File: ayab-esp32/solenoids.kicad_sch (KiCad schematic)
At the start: 10 parts, among them U301 MCP23017_SS

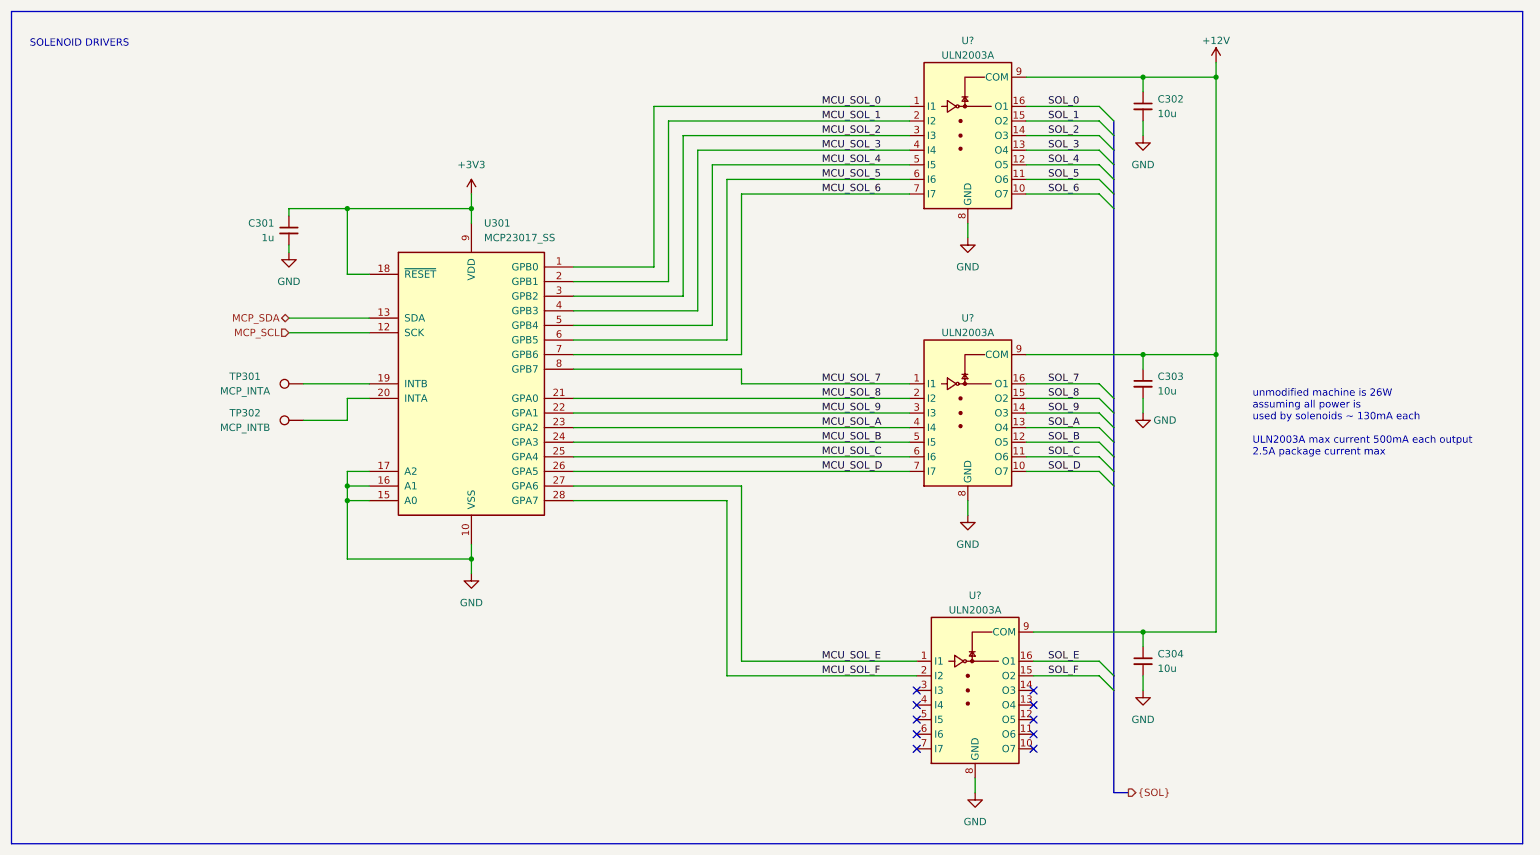
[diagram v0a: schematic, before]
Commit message: add component selection, bom
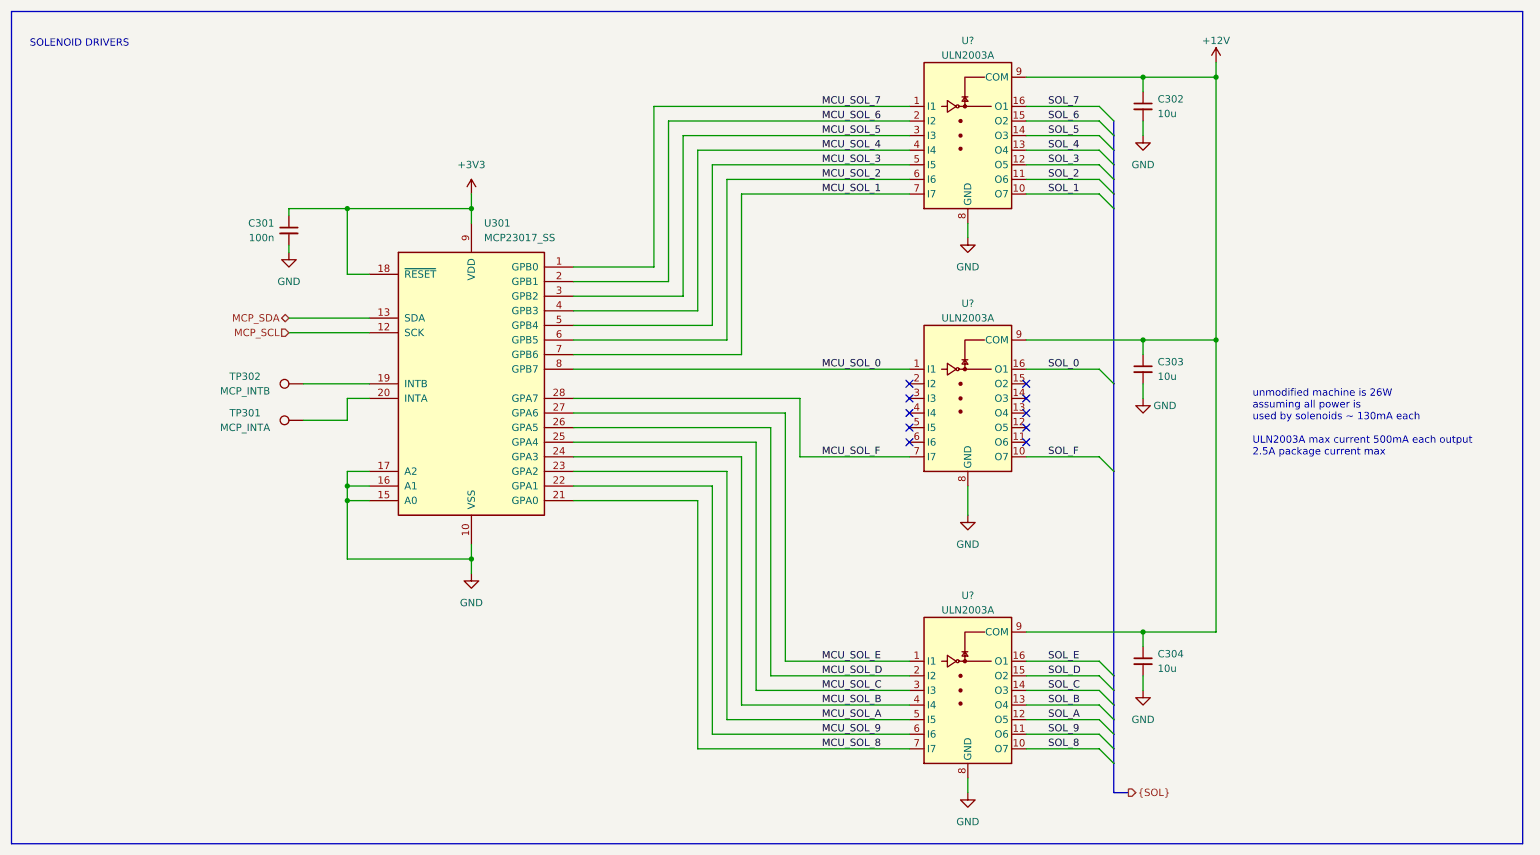
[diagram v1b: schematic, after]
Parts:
- C301: value 1u -> 100n; footprint (none) -> Capacitor_SMD:C_0603_1608Metric; symbol ayab-esp32:C_Small -> Library:C_Small; LCSC ID (none) -> C57112; OEM (none) -> FH (Guangdong Fenghua Advanced Tech); OEM PN (none) -> 0603B103K500NT; Package (none) -> 0603; Voltage rating (none) -> 24V X7R
- C302, C303, C304: footprint (none) -> Capacitor_SMD:C_0805_2012Metric; symbol ayab-esp32:C_Small -> Library:C_Small; LCSC ID (none) -> C15850; OEM (none) -> Samsung Electro-Mechanics; OEM PN (none) -> CL21A106KAYNNNE; Package (none) -> 0805; Voltage rating (none) -> 24V X5R
- TP301, TP302: footprint (none) -> TestPoint:TestPoint_Pad_D2.0mm; symbol ayab-esp32:TestPoint -> Library:TestPoint; now left out of the parts list
- U301: symbol ayab-esp32:MCP23017_SS -> Library:MCP23017_SS; LCSC ID (none) -> C506653; OEM (none) -> Microchip Tech; OEM PN (none) -> MCP23017-E/SS; Package (none) -> SSOP-28
- U? (x3): symbol ayab-esp32:ULN2003A -> Library:ULN2003A; LCSC ID (none) -> C7512; OEM (none) -> Texas Instruments; OEM PN (none) -> ULN2003ADR; Package (none) -> SOIC-16
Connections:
- net MCU_SOL_0: now also U301.8 (GPB7), U?.1 (I1); no longer U301.1 (GPB0), U?.1 (I1)
- net MCU_SOL_1: now also U301.7 (GPB6), U?.7 (I7); no longer U301.2 (GPB1), U?.2 (I2)
- net MCU_SOL_2: now also U301.6 (GPB5), U?.6 (I6); no longer U301.3 (GPB2), U?.3 (I3)
- net MCU_SOL_3: now also U301.5 (GPB4), U?.5 (I5); no longer U301.4 (GPB3), U?.4 (I4)
- net MCU_SOL_4: now also U301.4 (GPB3), U?.4 (I4); no longer U301.5 (GPB4), U?.5 (I5)
- net MCU_SOL_5: now also U301.3 (GPB2), U?.3 (I3); no longer U301.6 (GPB5), U?.6 (I6)
- net MCU_SOL_6: now also U301.2 (GPB1), U?.2 (I2); no longer U301.7 (GPB6), U?.7 (I7)
- net MCU_SOL_7: now also U301.1 (GPB0), U?.1 (I1); no longer U301.8 (GPB7), U?.1 (I1)
- net MCU_SOL_8: now also U?.7 (I7); no longer U?.2 (I2)
- net MCU_SOL_9: now also U?.6 (I6); no longer U?.3 (I3)
- net MCU_SOL_A: now also U?.5 (I5); no longer U?.4 (I4)
- net MCU_SOL_B: now also U?.4 (I4); no longer U?.5 (I5)
- net MCU_SOL_C: now also U?.3 (I3); no longer U?.6 (I6)
- net MCU_SOL_D: now also U?.2 (I2); no longer U?.7 (I7)
- net MCU_SOL_F: now also U?.7 (I7); no longer U?.2 (I2)
- net SOL_0: now also U?.16 (O1); no longer U?.16 (O1)
- net SOL_1: now also U?.10 (O7); no longer U?.15 (O2)
- net SOL_2: now also U?.11 (O6); no longer U?.14 (O3)
- net SOL_3: now also U?.12 (O5); no longer U?.13 (O4)
- net SOL_4: now also U?.13 (O4); no longer U?.12 (O5)
- net SOL_5: now also U?.14 (O3); no longer U?.11 (O6)
- net SOL_6: now also U?.15 (O2); no longer U?.10 (O7)
- net SOL_7: now also U?.16 (O1); no longer U?.16 (O1)
- net SOL_8: now also U?.10 (O7); no longer U?.15 (O2)
- net SOL_9: now also U?.11 (O6); no longer U?.14 (O3)
- net SOL_A: now also U?.12 (O5); no longer U?.13 (O4)
- net SOL_B: now also U?.13 (O4); no longer U?.12 (O5)
- net SOL_C: now also U?.14 (O3); no longer U?.11 (O6)
- net SOL_D: now also U?.15 (O2); no longer U?.10 (O7)
- net SOL_F: now also U?.10 (O7); no longer U?.15 (O2)
- net at U301.19 (INTB): now also TP302.1; no longer TP301.1
- net at U301.20 (INTA): now also TP301.1; no longer TP302.1
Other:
- moved on the sheet: C303, TP301, TP302, U?

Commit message: review ZVD P-ch MOSFET and resistors
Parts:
- C301, C302, C303, C304: symbol Library:C_Small -> ayab-lib:C_Small
- TP301, TP302: symbol Library:TestPoint -> ayab-lib:TestPoint
- U301: symbol Library:MCP23017_SS -> ayab-lib:MCP23017_SS
- U? (x3): symbol Library:ULN2003A -> ayab-lib:ULN2003A
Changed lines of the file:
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@@
     )
   )
-  (symbol (lib_id "Library:C_Small") (at 214.63 129.54 0) (unit 1)
+  (symbol (lib_id "ayab-lib:C_Small") (at 214.63 129.54 0) (unit 1)
     (in_bom yes) (on_board yes) (dnp no)
     (property "Reference" "C304" (at 217.17 128.2763 0)
@@
     )
   )
-  (symbol (lib_id "Library:C_Small") (at 214.63 33.02 0) (unit 1)
+  (symbol (lib_id "ayab-lib:C_Small") (at 214.63 33.02 0) (unit 1)
     (in_bom yes) (on_board yes) (dnp no)
     (property "Reference" "C302" (at 217.17 31.7563 0)
@@
     )
   )
-  (symbol (lib_id "Library:ULN2003A") (at 184.15 38.1 0) (unit 1)
+  (symbol (lib_id "ayab-lib:ULN2003A") (at 184.15 38.1 0) (unit 1)
     (in_bom yes) (on_board yes) (dnp no) (fields_autoplaced)
     (property "Reference" "U?" (at 184.15 21.59 0)
@@
     )
   )
-  (symbol (lib_id "Library:C_Small") (at 66.04 54.61 0) (mirror y) (unit 1)
+  (symbol (lib_id "ayab-lib:C_Small") (at 66.04 54.61 0) (mirror y) (unit 1)
     (in_bom yes) (on_board yes) (dnp no)
     (property "Reference" "C301" (at 63.5 53.3463 0)
@@
     )
   )
-  (symbol (lib_id "Library:C_Small") (at 214.63 78.74 0) (unit 1)
+  (symbol (lib_id "ayab-lib:C_Small") (at 214.63 78.74 0) (unit 1)
     (in_bom yes) (on_board yes) (dnp no)
     (property "Reference" "C303" (at 217.17 77.4763 0)
@@
     )
   )
-  (symbol (lib_id "Library:MCP23017_SS") (at 97.79 81.28 0) (unit 1)
+  (symbol (lib_id "ayab-lib:MCP23017_SS") (at 97.79 81.28 0) (unit 1)
     (in_bom yes) (on_board yes) (dnp no) (fields_autoplaced)
     (property "Reference" "U301" (at 99.9841 53.34 0)
@@
     )
   )
-  (symbol (lib_id "Library:ULN2003A") (at 184.15 83.82 0) (unit 1)
+  (symbol (lib_id "ayab-lib:ULN2003A") (at 184.15 83.82 0) (unit 1)
     (in_bom yes) (on_board yes) (dnp no) (fields_autoplaced)
     (property "Reference" "U?" (at 184.15 67.31 0)
@@
     )
   )
-  (symbol (lib_id "Library:TestPoint") (at 68.58 87.63 90) (unit 1)
+  (symbol (lib_id "ayab-lib:TestPoint") (at 68.58 87.63 90) (unit 1)
     (in_bom no) (on_board yes) (dnp no)
     (property "Reference" "TP301" (at 58.42 86.36 90)
@@
     )
   )
-  (symbol (lib_id "Library:ULN2003A") (at 184.15 134.62 0) (unit 1)
+  (symbol (lib_id "ayab-lib:ULN2003A") (at 184.15 134.62 0) (unit 1)
     (in_bom yes) (on_board yes) (dnp no) (fields_autoplaced)
     (property "Reference" "U?" (at 184.15 118.11 0)
@@
     )
   )
-  (symbol (lib_id "Library:TestPoint") (at 68.58 81.28 90) (unit 1)
+  (symbol (lib_id "ayab-lib:TestPoint") (at 68.58 81.28 90) (unit 1)
     (in_bom no) (on_board yes) (dnp no)
     (property "Reference" "TP302" (at 58.42 80.01 90)

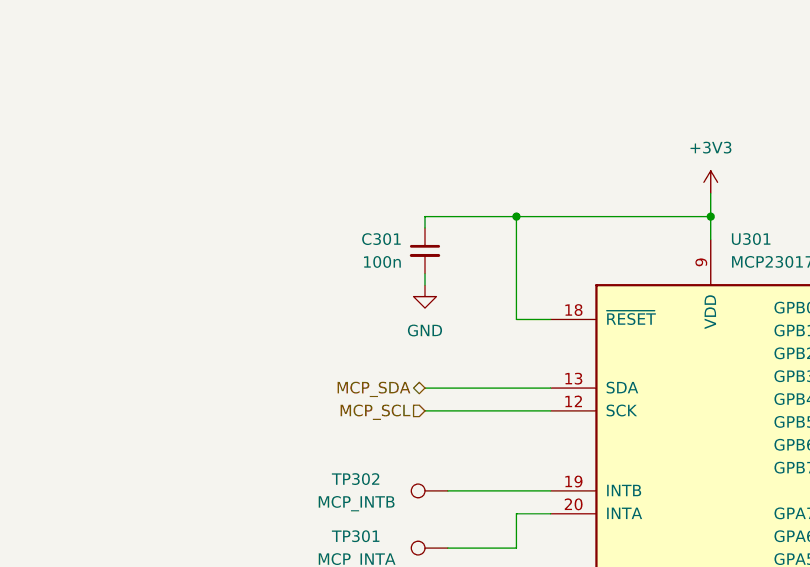
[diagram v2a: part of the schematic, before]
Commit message: first draft layout DRC clean
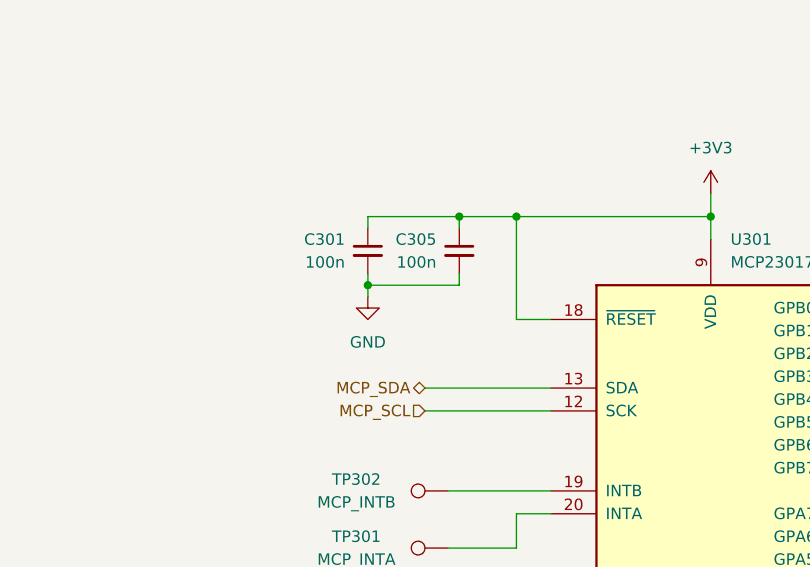
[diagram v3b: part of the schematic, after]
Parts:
- added C305: 100n, Capacitor_SMD:C_0603_1608Metric, symbol ayab-lib:C_Small
- TP301, TP302: footprint TestPoint:TestPoint_Pad_D2.0mm -> TestPoint:TestPoint_Pad_D1.0mm
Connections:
- net +3V3: now also C305.1
- net GND: now also C305.2
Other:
- moved on the sheet: C301
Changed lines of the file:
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@@
   (junction (at 97.79 111.76) (diameter 0) (color 0 0 0 0)
   )
+  (junction (at 59.69 58.42) (diameter 0) (color 0 0 0 0)
+  )
   (junction (at 76.2 101.6) (diameter 0) (color 0 0 0 0)
+  )
+  (junction (at 69.85 50.8) (diameter 0) (color 0 0 0 0)
   )
   (junction (at 227.33 73.66) (diameter 0) (color 0 0 0 0)
@@
     (stroke (width 0) (type default))
   )
+  (wire (pts (xy 69.85 57.15) (xy 69.85 58.42))
+    (stroke (width 0) (type default))
+  )
   (bus (pts (xy 209.55 96.52) (xy 209.55 132.08))
     (stroke (width 0) (type default))
@@
     (stroke (width 0) (type default))
   )
+  (wire (pts (xy 59.69 58.42) (xy 59.69 59.69))
+    (stroke (width 0) (type default))
+  )
   (wire (pts (xy 194.31 73.66) (xy 214.63 73.66))
     (stroke (width 0) (type default))
@@
     (stroke (width 0) (type default))
   )
-  (wire (pts (xy 66.04 50.8) (xy 66.04 52.07))
+  (wire (pts (xy 59.69 50.8) (xy 59.69 52.07))
     (stroke (width 0) (type default))
   )
@@
     (stroke (width 0) (type default))
   )
-  (wire (pts (xy 76.2 50.8) (xy 66.04 50.8))
+  (wire (pts (xy 76.2 50.8) (xy 69.85 50.8))
     (stroke (width 0) (type default))
   )
@@
     (stroke (width 0) (type default))
   )
+  (wire (pts (xy 69.85 50.8) (xy 69.85 52.07))
+    (stroke (width 0) (type default))
+  )
   (wire (pts (xy 227.33 73.66) (xy 227.33 27.94))
     (stroke (width 0) (type default))
@@
     (stroke (width 0) (type default))
   )
+  (wire (pts (xy 69.85 58.42) (xy 59.69 58.42))
+    (stroke (width 0) (type default))
+  )
   (wire (pts (xy 184.15 149.86) (xy 184.15 152.4))
     (stroke (width 0) (type default))
@@
     (stroke (width 0) (type default))
   )
+  (wire (pts (xy 69.85 50.8) (xy 59.69 50.8))
+    (stroke (width 0) (type default))
+  )
   (bus (pts (xy 209.55 40.64) (xy 209.55 43.18))
     (stroke (width 0) (type default))
@@
     (stroke (width 0) (type default))
   )
-  (wire (pts (xy 66.04 57.15) (xy 66.04 58.42))
+  (wire (pts (xy 59.69 57.15) (xy 59.69 58.42))
     (stroke (width 0) (type default))
   )
@@
         (path "/ad16b75f-afc8-4717-a7c6-8dd7b69a18e2/5c12a608-dfd1-46fe-96db-4ec512a20774"
           (reference "C304") (unit 1)
+        )
+      )
+    )
+  )
+  (symbol (lib_id "ayab-lib:C_Small") (at 69.85 54.61 0) (mirror y) (unit 1)
+    (in_bom yes) (on_board yes) (dnp no)
+    (property "Reference" "C305" (at 67.31 53.3463 0)
+      (effects (font (size 1.27 1.27)) (justify left))
+    )
+    (property "Value" "100n" (at 67.31 55.8863 0)
+      (effects (font (size 1.27 1.27)) (justify left))
+    )
+    (property "Footprint" "Capacitor_SMD:C_0603_1608Metric" (at 69.85 54.61 0)
+      (effects (font (size 1.27 1.27)) hide)
+    )
+    (property "Datasheet" "~" (at 69.85 54.61 0)
+      (effects (font (size 1.27 1.27)) hide)
+    )
+    (property "Package" "0603" (at 69.85 54.61 0)
+      (effects (font (size 1.27 1.27)) hide)
+    )
+    (property "Voltage rating" "24V X7R" (at 69.85 54.61 0)
+      (effects (font (size 1.27 1.27)) hide)
+    )
+    (property "LCSC ID" "C57112" (at 69.85 54.61 0)
+      (effects (font (size 1.27 1.27)) hide)
+    )
+    (property "OEM PN" "0603B103K500NT" (at 69.85 54.61 0)
+      (effects (font (size 1.27 1.27)) hide)
+    )
+    (property "OEM" "FH (Guangdong Fenghua Advanced Tech)" (at 69.85 54.61 0)
+      (effects (font (size 1.27 1.27)) hide)
+    )
+    (pin "1")
+    (pin "2")
+    (instances
+      (project "ayab-esp32"
+        (path "/ad16b75f-afc8-4717-a7c6-8dd7b69a18e2/5c12a608-dfd1-46fe-96db-4ec512a20774"
+          (reference "C305") (unit 1)
         )
       )
@@
     )
   )
-  (symbol (lib_id "ayab-lib:C_Small") (at 66.04 54.61 0) (mirror y) (unit 1)
+  (symbol (lib_id "ayab-lib:C_Small") (at 59.69 54.61 0) (mirror y) (unit 1)
     (in_bom yes) (on_board yes) (dnp no)
-    (property "Reference" "C301" (at 63.5 53.3463 0)
+    (property "Reference" "C301" (at 57.15 53.3463 0)
       (effects (font (size 1.27 1.27)) (justify left))
     )
-    (property "Value" "100n" (at 63.5 55.8863 0)
+    (property "Value" "100n" (at 57.15 55.8863 0)
       (effects (font (size 1.27 1.27)) (justify left))
     )
-    (property "Footprint" "Capacitor_SMD:C_0603_1608Metric" (at 66.04 54.61 0)
-      (effects (font (size 1.27 1.27)) hide)
-    )
-    (property "Datasheet" "~" (at 66.04 54.61 0)
-      (effects (font (size 1.27 1.27)) hide)
-    )
-    (property "Package" "0603" (at 66.04 54.61 0)
-      (effects (font (size 1.27 1.27)) hide)
-    )
-    (property "Voltage rating" "24V X7R" (at 66.04 54.61 0)
-      (effects (font (size 1.27 1.27)) hide)
-    )
-    (property "LCSC ID" "C57112" (at 66.04 54.61 0)
-      (effects (font (size 1.27 1.27)) hide)
-    )
-    (property "OEM PN" "0603B103K500NT" (at 66.04 54.61 0)
-      (effects (font (size 1.27 1.27)) hide)
-    )
-    (property "OEM" "FH (Guangdong Fenghua Advanced Tech)" (at 66.04 54.61 0)
+    (property "Footprint" "Capacitor_SMD:C_0603_1608Metric" (at 59.69 54.61 0)
+      (effects (font (size 1.27 1.27)) hide)
+    )
+    (property "Datasheet" "~" (at 59.69 54.61 0)
+      (effects (font (size 1.27 1.27)) hide)
+    )
+    (property "Package" "0603" (at 59.69 54.61 0)
+      (effects (font (size 1.27 1.27)) hide)
+    )
+    (property "Voltage rating" "24V X7R" (at 59.69 54.61 0)
+      (effects (font (size 1.27 1.27)) hide)
+    )
+    (property "LCSC ID" "C57112" (at 59.69 54.61 0)
+      (effects (font (size 1.27 1.27)) hide)
+    )
+    (property "OEM PN" "0603B103K500NT" (at 59.69 54.61 0)
+      (effects (font (size 1.27 1.27)) hide)
+    )
+    (property "OEM" "FH (Guangdong Fenghua Advanced Tech)" (at 59.69 54.61 0)
       (effects (font (size 1.27 1.27)) hide)
     )
@@
     )
   )
-  (symbol (lib_id "power:GND") (at 66.04 58.42 0) (mirror y) (unit 1)
+  (symbol (lib_id "power:GND") (at 59.69 59.69 0) (mirror y) (unit 1)
     (in_bom yes) (on_board yes) (dnp no)
-    (property "Reference" "#PWR0104" (at 66.04 64.77 0)
-      (effects (font (size 1.27 1.27)) hide)
-    )
-    (property "Value" "GND" (at 66.04 63.5 0)
-      (effects (font (size 1.27 1.27)))
-    )
-    (property "Footprint" "" (at 66.04 58.42 0)
-      (effects (font (size 1.27 1.27)) hide)
-    )
-    (property "Datasheet" "" (at 66.04 58.42 0)
+    (property "Reference" "#PWR0104" (at 59.69 66.04 0)
+      (effects (font (size 1.27 1.27)) hide)
+    )
+    (property "Value" "GND" (at 59.69 64.77 0)
+      (effects (font (size 1.27 1.27)))
+    )
+    (property "Footprint" "" (at 59.69 59.69 0)
+      (effects (font (size 1.27 1.27)) hide)
+    )
+    (property "Datasheet" "" (at 59.69 59.69 0)
       (effects (font (size 1.27 1.27)) hide)
     )
@@
       (effects (font (size 1.27 1.27)))
     )
-    (property "Footprint" "TestPoint:TestPoint_Pad_D2.0mm" (at 68.58 82.55 0)
+    (property "Footprint" "TestPoint:TestPoint_Pad_D1.0mm" (at 68.58 82.55 0)
       (effects (font (size 1.27 1.27)) hide)
     )
@@
       (effects (font (size 1.27 1.27)))
     )
-    (property "Footprint" "TestPoint:TestPoint_Pad_D2.0mm" (at 68.58 76.2 0)
-      (effects (font (size 1.27 1.27)) hide)
-    )
+    (property "Footprint" "TestPoint:TestPoint_Pad_D1.0mm" (at 68.58 76.2 0)
+      (effects (font (size 1.27 1.27)) hide)
+    )

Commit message: add mouser parts list
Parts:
- C301, C305: Mouser PN (none) -> 187-CL10B104MB8NNNC
- C302, C303, C304: Mouser PN (none) -> 963-TMK212BBJ106KG-T
- U301: Mouser PN (none) -> 579-MCP23017T-E/SS
- U? (x3): Mouser PN (none) -> 595-ULN2003ANSRE4
